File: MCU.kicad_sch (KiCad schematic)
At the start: 16 parts, among them Q1 1 DMN62D0UW-7, U2 STM32F405RGT6, Y1 8Mhz

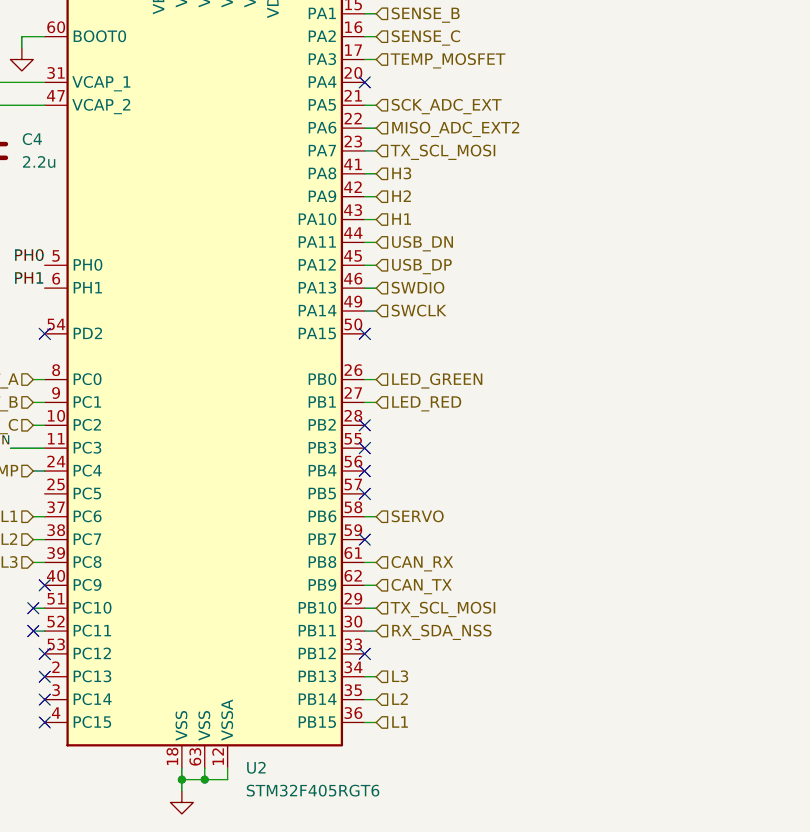
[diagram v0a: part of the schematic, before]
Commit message: Changed jst connectors
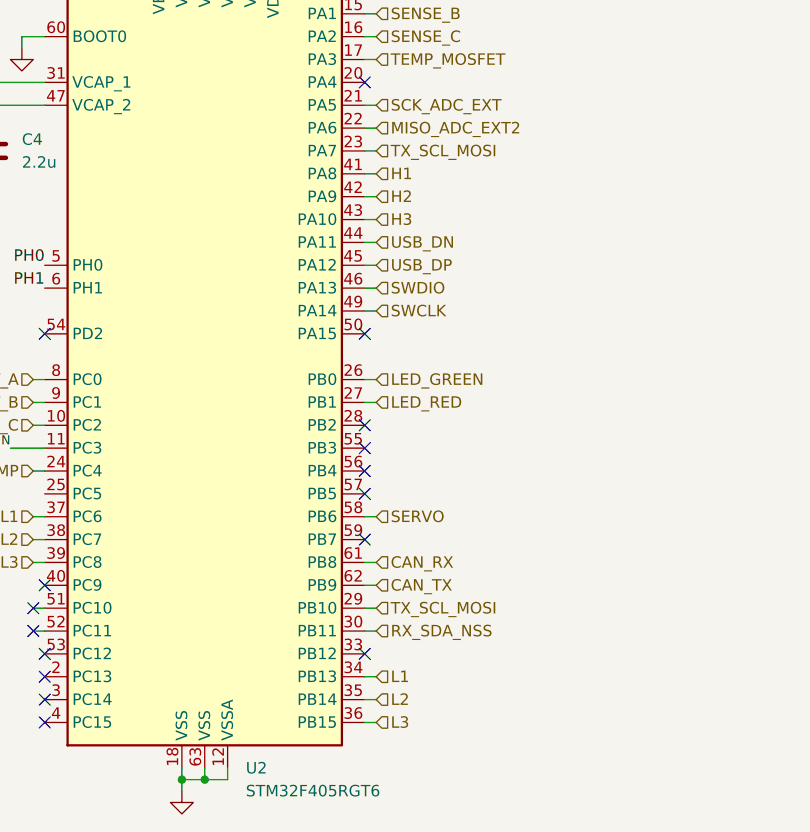
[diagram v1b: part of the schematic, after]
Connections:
- net H1: now also U2.41 (PA8); no longer U2.43 (PA10)
- net H3: now also U2.43 (PA10); no longer U2.41 (PA8)
- net L1: now also U2.34 (PB13); no longer U2.36 (PB15)
- net L3: now also U2.36 (PB15); no longer U2.34 (PB13)
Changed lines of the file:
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@@
     )
+  )
+  (hierarchical_label "H3" (shape input) (at 149.86 72.39 0)
+    (effects (font (size 1.27 1.27)) (justify left))
   )
   (hierarchical_label "SENSE_B" (shape input) (at 149.86 49.53 0)
@@
     (effects (font (size 1.27 1.27)) (justify left))
   )
-  (hierarchical_label "L1" (shape input) (at 149.86 128.27 0)
-    (effects (font (size 1.27 1.27)) (justify left))
-  )
   (hierarchical_label "NRST" (shape input) (at 78.74 46.99 180)
     (effects (font (size 1.27 1.27)) (justify right))
@@
     (effects (font (size 1.27 1.27)) (justify left))
   )
-  (hierarchical_label "L3" (shape input) (at 149.86 123.19 0)
+  (hierarchical_label "L3" (shape input) (at 149.86 128.27 0)
     (effects (font (size 1.27 1.27)) (justify left))
   )
@@
     (effects (font (size 1.27 1.27)) (justify left))
   )
+  (hierarchical_label "H1" (shape input) (at 149.86 67.31 0)
+    (effects (font (size 1.27 1.27)) (justify left))
+  )
   (hierarchical_label "USB_DP" (shape input) (at 149.86 77.47 0)
     (effects (font (size 1.27 1.27)) (justify left))
@@
     (effects (font (size 1.27 1.27)) (justify left))
   )
-  (hierarchical_label "H1" (shape input) (at 149.86 72.39 0)
+  (hierarchical_label "TX_SCL_MOSI" (shape input) (at 149.86 64.77 0)
     (effects (font (size 1.27 1.27)) (justify left))
   )
-  (hierarchical_label "TX_SCL_MOSI" (shape input) (at 149.86 64.77 0)
+  (hierarchical_label "L1" (shape input) (at 149.86 123.19 0)
     (effects (font (size 1.27 1.27)) (justify left))
   )
@@
     (effects (font (size 1.27 1.27)) (justify right))
   )
-  (hierarchical_label "H3" (shape input) (at 149.86 67.31 0)
-    (effects (font (size 1.27 1.27)) (justify left))
-  )
   (hierarchical_label "ADC_TEMP" (shape input) (at 111.76 100.33 180)

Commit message: what changed?
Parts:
- C1, C2: LCSC (none) -> C107110
- C10, C11, C3, C4, C5, C7, C8, C9: value 2.2u -> 2u2
- C50: LCSC (none) -> C49678
- Q1: LCSC (none) -> C156342
- R5: LCSC (none) -> C113306
- R6: LCSC (none) -> C2907234
- Y1: LCSC (none) -> C2924619
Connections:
- no-connect marks 16 -> 17
